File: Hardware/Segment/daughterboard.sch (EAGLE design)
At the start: 71 parts, among them IC1 PBQ79656PAPTQ1, X1 5566-12, X2 5566-12, X3 5566-16

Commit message: LDOIN
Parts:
- added CCB20: 0.1uf, capacitor-wima:C2.5/2
- added CCB21: 0.22uf, capacitor-wima:C2.5/2
- added Q1: (no value), semicon-smd-ipc:NPN-TRANSISTIOR-2COLSOT143
- added RVC16: 49, rcl:R-US_R0603
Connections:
- removed net N$29: RCB10.1, RCB11.2, X2-11.S
- new net BATC: RCB10.1, RCB11.2, RVC16.2, X2-11.S
- new net GND: CCB21.1
- new net LDOIN: CCB20.2, IC1.LDOIN, Q1.E
- new net N$65: CCB21.2, Q1.C, RVC16.1
- new net NPNB: IC1.NPNB, Q1.B
- net GNDN: now also CCB20.1
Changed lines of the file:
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@@
 <part name="CCB18" library="capacitor-wima" library_urn="urn:adsk.eagle:library:116" deviceset="C" device="2.5/2" package3d_urn="urn:adsk.eagle:package:5415/1" value="220pf"/>
 <part name="CCB19" library="capacitor-wima" library_urn="urn:adsk.eagle:library:116" deviceset="C" device="2.5/2" package3d_urn="urn:adsk.eagle:package:5415/1" value="220pf"/>
+<part name="CCB20" library="capacitor-wima" library_urn="urn:adsk.eagle:library:116" deviceset="C" device="2.5/2" package3d_urn="urn:adsk.eagle:package:5415/1" value="0.1uf"/>
+<part name="Q1" library="semicon-smd-ipc" library_urn="urn:adsk.eagle:library:353" deviceset="NPN-TRANSISTIOR-2COL" device="SOT143" package3d_urn="urn:adsk.eagle:package:26315/2"/>
+<part name="RVC16" library="rcl" library_urn="urn:adsk.eagle:library:334" deviceset="R-US_" device="R0603" package3d_urn="urn:adsk.eagle:package:23555/3" value="49"/>
+<part name="CCB21" library="capacitor-wima" library_urn="urn:adsk.eagle:library:116" deviceset="C" device="2.5/2" package3d_urn="urn:adsk.eagle:package:5415/1" value="0.22uf"/>
+<part name="GND1" library="supply1" library_urn="urn:adsk.eagle:library:371" deviceset="GND" device=""/>
 </parts>
 <sheets>
@@
 <attribute name="NAME" x="170.561" y="6.096" size="1.778" layer="95" rot="R270"/>
 <attribute name="VALUE" x="165.481" y="6.096" size="1.778" layer="96" rot="R270"/>
+</instance>
+<instance part="CCB20" gate="G$1" x="116.84" y="7.62" smashed="yes" rot="R90">
+<attribute name="NAME" x="116.459" y="9.144" size="1.778" layer="95" rot="R90"/>
+<attribute name="VALUE" x="121.539" y="9.144" size="1.778" layer="96" rot="R90"/>
+</instance>
+<instance part="Q1" gate="G$1" x="127" y="-2.54" smashed="yes" rot="R180">
+<attribute name="NAME" x="137.16" y="-5.08" size="1.778" layer="95" rot="R180"/>
+<attribute name="VALUE" x="137.16" y="-7.62" size="1.778" layer="96" rot="R180"/>
+</instance>
+<instance part="RVC16" gate="G$1" x="109.22" y="-7.62" smashed="yes" rot="R180">
+<attribute name="NAME" x="113.03" y="-9.1186" size="1.778" layer="95" rot="R180"/>
+<attribute name="VALUE" x="113.03" y="-4.318" size="1.778" layer="96" rot="R180"/>
+</instance>
+<instance part="CCB21" gate="G$1" x="106.68" y="0" smashed="yes" rot="R90">
+<attribute name="NAME" x="106.299" y="1.524" size="1.778" layer="95" rot="R90"/>
+<attribute name="VALUE" x="111.379" y="1.524" size="1.778" layer="96" rot="R90"/>
+</instance>
+<instance part="GND1" gate="1" x="93.98" y="0" smashed="yes" rot="R270">
+<attribute name="VALUE" x="91.44" y="2.54" size="1.778" layer="96" rot="R270"/>
 </instance>
 </instances>
@@
 <pinref part="RVC10" gate="G$1" pin="2"/>
 <wire x1="71.12" y1="111.76" x2="71.12" y2="116.84" width="0.1524" layer="91"/>
-</segment>
-</net>
-<net name="N$29" class="0">
-<segment>
-<pinref part="RCB10" gate="G$1" pin="1"/>
-<wire x1="45.72" y1="119.38" x2="71.12" y2="119.38" width="0.1524" layer="91"/>
-<pinref part="X2" gate="-11" pin="S"/>
-<wire x1="45.72" y1="119.38" x2="45.72" y2="124.46" width="0.1524" layer="91"/>
-<junction x="45.72" y="119.38"/>
-<pinref part="RCB11" gate="G$1" pin="2"/>
-<wire x1="45.72" y1="124.46" x2="177.8" y2="124.46" width="0.1524" layer="91"/>
-<wire x1="177.8" y1="124.46" x2="177.8" y2="104.14" width="0.1524" layer="91"/>
 </segment>
 </net>
@@
 <junction x="175.26" y="20.32"/>
 </segment>
+<segment>
+<pinref part="CCB20" gate="G$1" pin="1"/>
+<wire x1="114.3" y1="7.62" x2="93.98" y2="7.62" width="0.1524" layer="91"/>
+<label x="101.6" y="10.16" size="1.778" layer="95" rot="R180"/>
+</segment>
 </net>
 <net name="N$46" class="0">
@@
 </segment>
 </net>
+<net name="N$65" class="0">
+<segment>
+<pinref part="Q1" gate="G$1" pin="C"/>
+<pinref part="RVC16" gate="G$1" pin="1"/>
+<wire x1="124.46" y1="-7.62" x2="116.84" y2="-7.62" width="0.1524" layer="91"/>
+<wire x1="116.84" y1="-7.62" x2="114.3" y2="-7.62" width="0.1524" layer="91"/>
+<wire x1="116.84" y1="-7.62" x2="116.84" y2="0" width="0.1524" layer="91"/>
+<junction x="116.84" y="-7.62"/>
+<wire x1="116.84" y1="0" x2="111.76" y2="0" width="0.1524" layer="91"/>
+<pinref part="CCB21" gate="G$1" pin="2"/>
+</segment>
+</net>
+<net name="BATC" class="0">
+<segment>
+<pinref part="RVC16" gate="G$1" pin="2"/>
+<wire x1="104.14" y1="-7.62" x2="93.98" y2="-7.62" width="0.1524" layer="91"/>
+<label x="93.98" y="-7.62" size="1.778" layer="95"/>
+</segment>
+<segment>
+<pinref part="RCB10" gate="G$1" pin="1"/>
+<wire x1="45.72" y1="119.38" x2="71.12" y2="119.38" width="0.1524" layer="91"/>
+<pinref part="X2" gate="-11" pin="S"/>
+<wire x1="45.72" y1="119.38" x2="45.72" y2="124.46" width="0.1524" layer="91"/>
+<junction x="45.72" y="119.38"/>
+<pinref part="RCB11" gate="G$1" pin="2"/>
+<wire x1="45.72" y1="124.46" x2="177.8" y2="124.46" width="0.1524" layer="91"/>
+<wire x1="177.8" y1="124.46" x2="177.8" y2="104.14" width="0.1524" layer="91"/>
+<wire x1="177.8" y1="124.46" x2="190.5" y2="124.46" width="0.1524" layer="91"/>
+<junction x="177.8" y="124.46"/>
+<label x="185.42" y="124.46" size="1.778" layer="95"/>
+</segment>
+</net>
+<net name="LDOIN" class="0">
+<segment>
+<pinref part="IC1" gate="G$1" pin="LDOIN"/>
+<wire x1="175.26" y1="27.94" x2="175.26" y2="22.86" width="0.1524" layer="91"/>
+<label x="175.26" y="22.86" size="1.778" layer="95" rot="R90"/>
+</segment>
+<segment>
+<pinref part="Q1" gate="G$1" pin="E"/>
+<wire x1="124.46" y1="2.54" x2="124.46" y2="7.62" width="0.1524" layer="91"/>
+<pinref part="CCB20" gate="G$1" pin="2"/>
+<wire x1="124.46" y1="7.62" x2="121.92" y2="7.62" width="0.1524" layer="91"/>
+<wire x1="124.46" y1="7.62" x2="137.16" y2="7.62" width="0.1524" layer="91"/>
+<junction x="124.46" y="7.62"/>
+<label x="129.54" y="7.62" size="1.778" layer="95"/>
+</segment>
+</net>
+<net name="NPNB" class="0">
+<segment>
+<pinref part="IC1" gate="G$1" pin="NPNB"/>
+<wire x1="177.8" y1="27.94" x2="177.8" y2="22.86" width="0.1524" layer="91"/>
+<label x="177.8" y="22.86" size="1.778" layer="95" rot="R90"/>
+</segment>
+<segment>
+<pinref part="Q1" gate="G$1" pin="B"/>
+<wire x1="129.54" y1="-2.54" x2="137.16" y2="-2.54" width="0.1524" layer="91"/>
+<label x="129.54" y="-2.54" size="1.778" layer="95"/>
+</segment>
+</net>
+<net name="GND" class="0">
+<segment>
+<pinref part="CCB21" gate="G$1" pin="1"/>
+<pinref part="GND1" gate="1" pin="GND"/>
+<wire x1="104.14" y1="0" x2="96.52" y2="0" width="0.1524" layer="91"/>
+</segment>
+</net>

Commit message: NPN
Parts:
- removed Q1: (no value), semicon-smd-ipc:NPN-TRANSISTIOR-2COLSOT143
- added T1: PBHV8115X, 115, transistor:BC868-NPN-SOT89-BCE
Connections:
- net N$49 renamed CVDD
- net LDOIN: now also T1.E; no longer Q1.E
- net N$65: now also T1.C; no longer Q1.C
- net NPNB: now also T1.B; no longer Q1.B
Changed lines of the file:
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@@
 <part name="CCB19" library="capacitor-wima" library_urn="urn:adsk.eagle:library:116" deviceset="C" device="2.5/2" package3d_urn="urn:adsk.eagle:package:5415/1" value="220pf"/>
 <part name="CCB20" library="capacitor-wima" library_urn="urn:adsk.eagle:library:116" deviceset="C" device="2.5/2" package3d_urn="urn:adsk.eagle:package:5415/1" value="0.1uf"/>
-<part name="Q1" library="semicon-smd-ipc" library_urn="urn:adsk.eagle:library:353" deviceset="NPN-TRANSISTIOR-2COL" device="SOT143" package3d_urn="urn:adsk.eagle:package:26315/2"/>
 <part name="RVC16" library="rcl" library_urn="urn:adsk.eagle:library:334" deviceset="R-US_" device="R0603" package3d_urn="urn:adsk.eagle:package:23555/3" value="49"/>
 <part name="CCB21" library="capacitor-wima" library_urn="urn:adsk.eagle:library:116" deviceset="C" device="2.5/2" package3d_urn="urn:adsk.eagle:package:5415/1" value="0.22uf"/>
-<part name="GND1" library="supply1" library_urn="urn:adsk.eagle:library:371" deviceset="GND" device=""/>
+<part name="T1" library="transistor" library_urn="urn:adsk.eagle:library:402" deviceset="*-NPN-" device="SOT89-BCE" package3d_urn="urn:adsk.eagle:package:29925/3" technology="BC868" value="PBHV8115X, 115"/>
 </parts>
 <sheets>
@@
 <attribute name="VALUE" x="121.539" y="9.144" size="1.778" layer="96" rot="R90"/>
 </instance>
-<instance part="Q1" gate="G$1" x="127" y="-2.54" smashed="yes" rot="R180">
-<attribute name="NAME" x="137.16" y="-5.08" size="1.778" layer="95" rot="R180"/>
-<attribute name="VALUE" x="137.16" y="-7.62" size="1.778" layer="96" rot="R180"/>
-</instance>
 <instance part="RVC16" gate="G$1" x="109.22" y="-7.62" smashed="yes" rot="R180">
 <attribute name="NAME" x="113.03" y="-9.1186" size="1.778" layer="95" rot="R180"/>
@@
 <attribute name="VALUE" x="111.379" y="1.524" size="1.778" layer="96" rot="R90"/>
 </instance>
-<instance part="GND1" gate="1" x="93.98" y="0" smashed="yes" rot="R270">
-<attribute name="VALUE" x="91.44" y="2.54" size="1.778" layer="96" rot="R270"/>
+<instance part="T1" gate="G$1" x="127" y="-2.54" smashed="yes" rot="R180">
+<attribute name="NAME" x="137.16" y="-10.16" size="1.778" layer="95" rot="R180"/>
+<attribute name="VALUE" x="137.16" y="-7.62" size="1.778" layer="96" rot="R180"/>
 </instance>
 </instances>
@@
 <pinref part="CCB20" gate="G$1" pin="1"/>
 <wire x1="114.3" y1="7.62" x2="93.98" y2="7.62" width="0.1524" layer="91"/>
-<label x="101.6" y="10.16" size="1.778" layer="95" rot="R180"/>
+<label x="93.98" y="7.62" size="1.778" layer="95"/>
 </segment>
 </net>
@@
 <pinref part="CCB13" gate="G$1" pin="2"/>
 <pinref part="IC1" gate="G$1" pin="NEG5V"/>
-</segment>
-</net>
-<net name="N$49" class="0">
-<segment>
-<pinref part="CCB14" gate="G$1" pin="2"/>
-<pinref part="IC1" gate="G$1" pin="CVDD"/>
-<wire x1="170.18" y1="27.94" x2="170.18" y2="43.18" width="0.1524" layer="91"/>
-<junction x="170.18" y="27.94"/>
-<pinref part="IC1" gate="G$1" pin="RX"/>
-<wire x1="170.18" y1="43.18" x2="190.5" y2="43.18" width="0.1524" layer="91"/>
 </segment>
 </net>
@@
 <net name="N$65" class="0">
 <segment>
-<pinref part="Q1" gate="G$1" pin="C"/>
 <pinref part="RVC16" gate="G$1" pin="1"/>
 <wire x1="124.46" y1="-7.62" x2="116.84" y2="-7.62" width="0.1524" layer="91"/>
@@
 <wire x1="116.84" y1="0" x2="111.76" y2="0" width="0.1524" layer="91"/>
 <pinref part="CCB21" gate="G$1" pin="2"/>
+<pinref part="T1" gate="G$1" pin="C"/>
 </segment>
 </net>
@@
 </segment>
 <segment>
-<pinref part="Q1" gate="G$1" pin="E"/>
 <wire x1="124.46" y1="2.54" x2="124.46" y2="7.62" width="0.1524" layer="91"/>
 <pinref part="CCB20" gate="G$1" pin="2"/>
@@
 <junction x="124.46" y="7.62"/>
 <label x="129.54" y="7.62" size="1.778" layer="95"/>
+<pinref part="T1" gate="G$1" pin="E"/>
 </segment>
 </net>
@@
 </segment>
 <segment>
-<pinref part="Q1" gate="G$1" pin="B"/>
 <wire x1="129.54" y1="-2.54" x2="137.16" y2="-2.54" width="0.1524" layer="91"/>
 <label x="129.54" y="-2.54" size="1.778" layer="95"/>
+<pinref part="T1" gate="G$1" pin="B"/>
+</segment>
+</net>
+<net name="CVDD" class="0">
+<segment>
+<pinref part="IC1" gate="G$1" pin="RX"/>
+<wire x1="190.5" y1="43.18" x2="170.18" y2="43.18" width="0.1524" layer="91"/>
+<pinref part="CCB14" gate="G$1" pin="2"/>
+<pinref part="IC1" gate="G$1" pin="CVDD"/>
+<wire x1="170.18" y1="43.18" x2="170.18" y2="27.94" width="0.1524" layer="91"/>
+<junction x="170.18" y="27.94"/>
 </segment>
 </net>
@@
 <segment>
 <pinref part="CCB21" gate="G$1" pin="1"/>
-<pinref part="GND1" gate="1" pin="GND"/>
-<wire x1="104.14" y1="0" x2="96.52" y2="0" width="0.1524" layer="91"/>
-</segment>
-</net>
+<wire x1="104.14" y1="0" x2="93.98" y2="0" width="0.1524" layer="91"/>
+<label x="93.98" y="0" size="1.778" layer="95"/>
+</segment>
+</net>

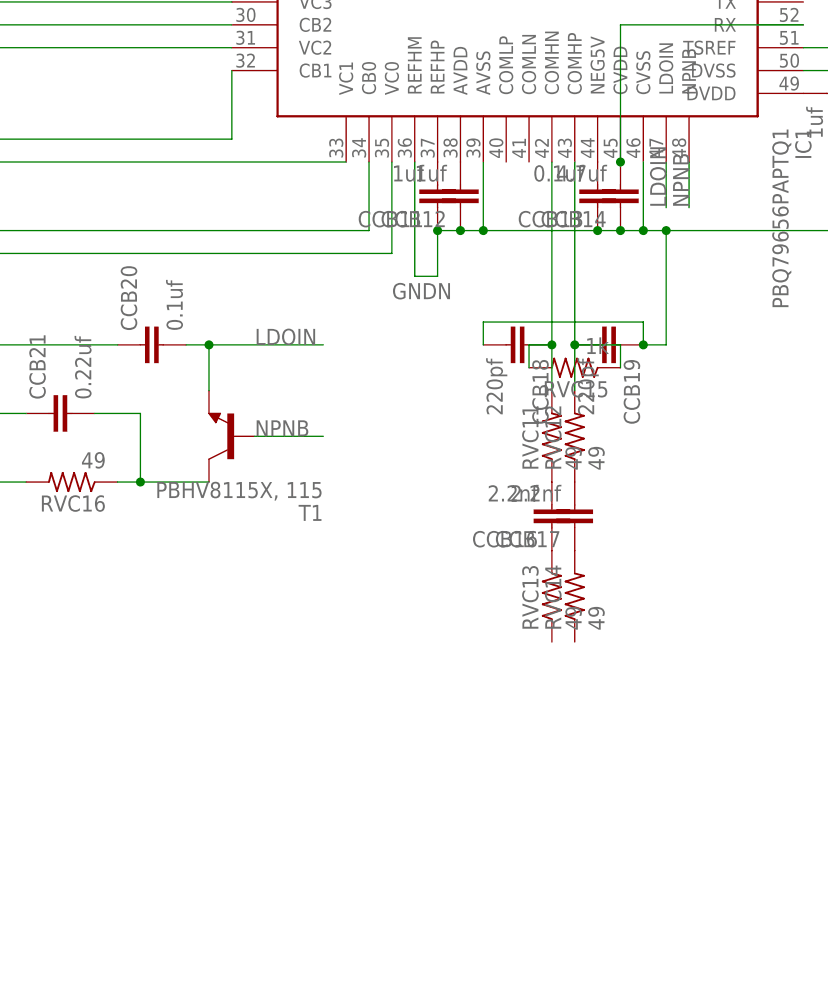
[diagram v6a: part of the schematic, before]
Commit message: added COMLP and COMLN connection
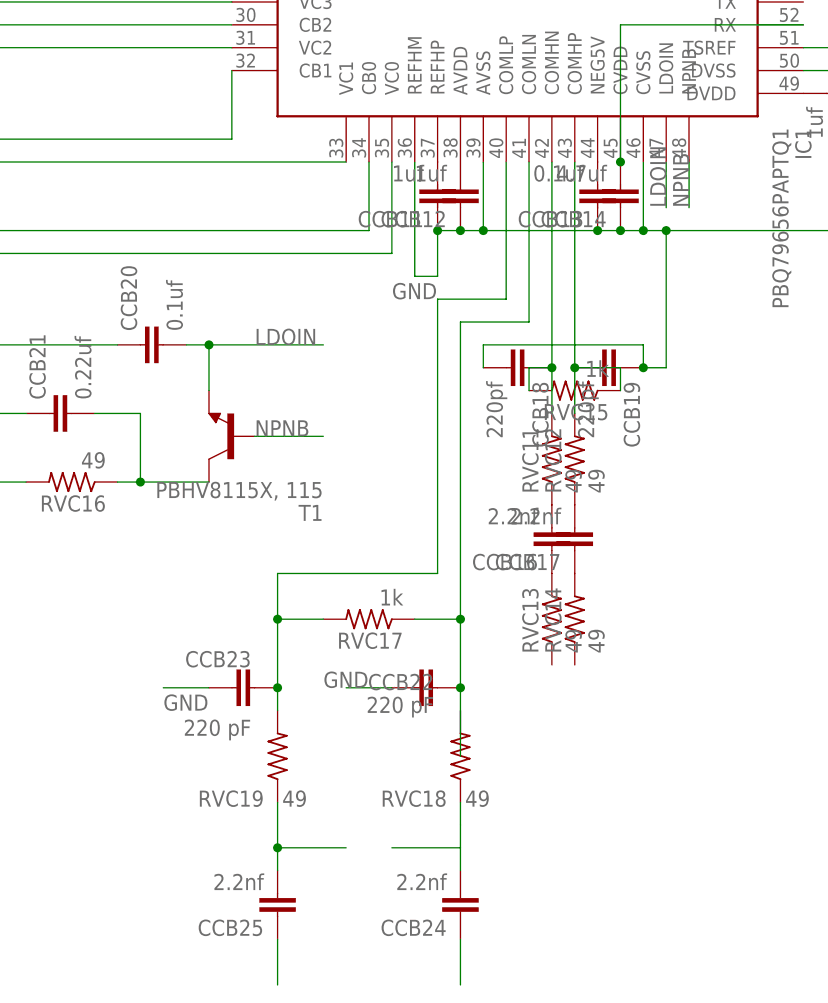
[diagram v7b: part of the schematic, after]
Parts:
- added CCB22, CCB23: 220 pF, capacitor-wima:C2.5/2
- added CCB24, CCB25: 2.2nf, capacitor-wima:C2.5/2
- added RVC17: 1k, rcl:R-US_R0603
- added RVC18, RVC19: 49, rcl:R-US_R0603
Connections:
- new net N$29: CCB22.2, IC1.COMLN, RVC17.1, RVC18.2
- new net N$49: CCB23.2, IC1.COMLP, RVC17.2, RVC19.2
- new net N$66: CCB25.1
- new net N$67: CCB25.2, RVC19.1
- new net N$68: CCB24.2, RVC18.1
- new net N$69: CCB24.1
- net GND: now also CCB11.1, CCB12.1, CCB13.1, CCB14.1, CCB15.1, CCB18.2, CCB19.1, CCB22.1, CCB23.1, IC1.AVSS, IC1.AVSS?, IC1.CVSS, IC1.DVSS, IC1.REFHM
- net GNDN: no longer CCB11.1, CCB12.1, CCB13.1, CCB14.1, CCB15.1, CCB18.2, CCB19.1, IC1.AVSS, IC1.AVSS?, IC1.CVSS, IC1.DVSS, IC1.REFHM
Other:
- moved on the sheet: CCB16, CCB17, CCB18, CCB19, RVC11, RVC12, RVC13, RVC14, RVC15

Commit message: Finished daughterboard schematic?
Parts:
- added C2, C3: 1 uF, capacitor-wima:C2.5/2
- added CCB26, CCB27, CCB28, CCB29, CCB30, CCB31, CCB32, CCB33, CCB34, CCB35, CCB52, CCB53, CCB54, CCB55, CCB56, CCB57, CCB58, CCB59, CCB60, CCB61, CVC10, CVC11, CVC12, CVC13, CVC14, CVC15, CVC16, CVC17, CVC18, CVC19, CVC20, CVC21, CVC22, CVC23, CVC24, CVC25, CVC26, CVC27, CVC28, CVC29: 0.47uf, capacitor-wima:C2.5/2
- added CCB36, CCB62: 10 nf, capacitor-wima:C2.5/2
- added CCB37, CCB38, CCB41, CCB63, CCB64, CCB67: 1uf, capacitor-wima:C2.5/2
- added CCB39, CCB46, CCB65, CCB68: 0.1uf, capacitor-wima:C2.5/2
- added CCB40, CCB66: 4.7uf, capacitor-wima:C2.5/2
- added CCB42, CCB43, CCB49, CCB50, CCB71, CCB72: 2.2nf, capacitor-wima:C2.5/2
- added CCB44, CCB45, CCB74, CCB75: 220pf, capacitor-wima:C2.5/2
- added CCB47, CCB69: 0.22uf, capacitor-wima:C2.5/2
- added CCB48, CCB51, CCB70, CCB73: 220 pF, capacitor-wima:C2.5/2
- added D1, D2, D3: ESDAVLC6-2BLY, ESDAVLC6-2BLY:ESDAVLC6-2BLY
- added IC2, IC3: PBQ79656PAPTQ1, PBQ79656PAPTQ1:PBQ79656PAPTQ1
- added R10, R11, R12, R13, R14, R15, R16, R17, R18, R19, R20, R21, R22, R23, R24, R9: 10k, rcl:R-US_R0603
- added RCB12, RCB13, RCB14, RCB15, RCB16, RCB17, RCB18, RCB19, RCB20, RCB21, RCB22, RCB24, RCB25, RCB26, RCB27, RCB28, RCB29, RCB30, RCB31, RCB32, RCB33, RCB34: 10, rcl:R-US_R0603
- added RCB23, RCB35: 30, rcl:R-US_R0603
- added RVC20, RVC21, RVC22, RVC23, RVC24, RVC25, RVC26, RVC27, RVC28, RVC29, RVC30, RVC40, RVC41, RVC42, RVC43, RVC44, RVC45, RVC46, RVC47, RVC48, RVC49, RVC50: 100, rcl:R-US_R0603
- added RVC31, RVC32, RVC33, RVC34, RVC36, RVC38, RVC39, RVC51, RVC53, RVC54: 49, rcl:R-US_R0603
- added RVC35, RVC37, RVC52, RVC55: 1k, rcl:R-US_R0603
- added T2, T3: PBHV8115X, 115, transistor:BC868-NPN-SOT89-BCE
- added X4, X5, X7, X8: 5566-12, con-molex:5566-12
- added X6, X9: 5566-16, con-molex:5566-16
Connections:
- new net BATC-1: RCB21.1, RCB23.2, RCB33.1, RCB35.2, RVC36.2, RVC51.2, X5-11.S, X8-11.S
- new net COMMN: CCB74.1, IC3.COMLN, RVC33.1, RVC55.2
- new net COMMP: CCB75.2, IC3.COMLP, RVC34.1, RVC55.1
- new net CVDD-1: CCB40.2, IC2.CVDD, IC2.RX
- new net CVDD2: CCB66.2, IC3.CVDD, IC3.RX
- new net GND-1: CCB37.1, CCB38.1, CCB39.1, CCB40.1, CCB41.1, CCB44.2, CCB45.1, CCB47.1, CCB48.1, CCB51.1, CCB63.1, CCB64.1, CCB65.1, CCB66.1, CCB67.1, CCB69.1, CCB70.1, CCB73.1, CCB74.2, CCB75.1, D2.3, D3.3, IC2.AVSS, IC2.AVSS?, IC2.CVSS, IC2.DVSS, IC2.REFHM, IC3.AVSS, IC3.AVSS?, IC3.CVSS, IC3.DVSS, IC3.REFHM
- new net GND1-1: C2.1, C3.1, CCB36.1, CCB62.1, RCB22.1, RCB34.1, X5-1.S, X6-10.S, X6-11.S, X6-12.S, X6-13.S, X6-14.S, X6-15.S, X6-16.S, X6-9.S, X8-1.S, X9-10.S, X9-11.S, X9-12.S, X9-13.S, X9-14.S, X9-15.S, X9-16.S, X9-9.S
- new net GNDN-1: CCB46.1, CCB68.1
- new net LDOIN-1: CCB46.2, CCB68.2, IC2.LDOIN, IC3.LDOIN, T2.E, T3.E
- new net N$100: CCB35.2, IC2.CB0, RCB22.2
- new net N$101: CVC19.2, RVC30.1, X4-1.S
- new net N$102: CVC10.2, CVC19.1, RVC20.1, X4-2.S
- new net N$103: CVC10.1, CVC11.2, RVC21.1, X4-3.S
- new net N$104: CVC11.1, CVC12.2, RVC22.1, X4-4.S
- new net N$105: CVC12.1, CVC13.2, RVC23.1, X4-5.S
- new net N$106: CVC13.1, CVC14.2, RVC24.1, X4-6.S
- new net N$107: CVC14.1, CVC15.2, RVC25.1, X4-7.S
- new net N$108: CVC15.1, CVC16.2, RVC26.1, X4-8.S
- new net N$109: CVC16.1, CVC17.2, RVC27.1, X4-9.S
- new net N$110: CVC17.1, CVC18.2, RVC28.1, X4-10.S
- new net N$111: CVC18.1, RVC29.1, X4-11.S
- new net N$112: CCB36.2, IC2.BAT, IC2.CB11, IC2.CB12, IC2.CB13, IC2.CB14, IC2.CB15, IC2.CB16, IC2.VC11, IC2.VC12, IC2.VC13, IC2.VC14, IC2.VC15, IC2.VC16, RCB23.1
- new net N$113: CCB37.2, IC2.REFHP
- new net N$114: CCB38.2, IC2.AVDD
- new net N$115: CCB39.2, IC2.NEG5V
- new net N$116: CCB41.2, IC2.DVDD
- new net N$117: IC2.GPIO1, R16.2, X6-1.S
- new net N$118: IC2.GPIO2, R15.2, X6-2.S
- new net N$119: IC2.GPIO3, R14.2, X6-3.S
- new net N$120: IC2.GPIO4, R13.2, X6-4.S
- new net N$121: IC2.GPIO5, R12.2, X6-5.S
- new net N$122: IC2.GPIO6, R11.2, X6-6.S
- new net N$123: IC2.GPIO7, R10.2, X6-7.S
- new net N$124: IC2.GPIO8, R9.2, X6-8.S
- new net N$125: C2.2, IC2.TSREF, R10.1, R11.1, R12.1, R13.1, R14.1, R15.1, R16.1, R9.1
- new net N$126: CCB44.1, IC2.COMHN, RVC31.2, RVC35.2
- new net N$127: CCB45.2, IC2.COMHP, RVC32.2, RVC35.1
- new net N$128: CCB42.2, RVC31.1
- new net N$129: CCB43.2, RVC32.1
- new net N$130: CCB42.1, RVC33.2
- new net N$131: CCB43.1, RVC34.2
- new net N$132: CCB47.2, RVC36.1, T2.C
- new net N$133: CCB48.2, IC2.COMLN, RVC37.1, RVC38.2
- new net N$134: CCB51.2, IC2.COMLP, RVC37.2, RVC39.2
- new net N$135: CCB50.2, D2.2, RVC39.1
- new net N$136: CCB49.2, D2.1, RVC38.1
- new net N$137: CCB49.1
- new net N$138: CCB50.1
- new net N$139: IC3.VC1, RVC40.2
- new net N$140: CCB52.2, CCB61.1, IC3.CB1, RCB24.2
- new net N$141: IC3.VC2, RVC41.2
- new net N$142: CCB52.1, CCB53.2, IC3.CB2, RCB25.2
- new net N$143: RCB25.1, X8-3.S
- new net N$144: RCB24.1, X8-2.S
- new net N$145: CCB53.1, CCB54.2, IC3.CB3, RCB26.2
- new net N$146: RCB26.1, X8-4.S
- new net N$147: IC3.VC3, RVC42.2
- new net N$148: IC3.VC4, RVC43.2
- new net N$149: RCB27.1, X8-5.S
- new net N$150: CCB54.1, CCB55.2, IC3.CB4, RCB27.2
- new net N$151: IC3.VC5, RVC44.2
- new net N$152: RCB28.1, X8-6.S
- new net N$153: CCB55.1, CCB56.2, IC3.CB5, RCB28.2
- new net N$154: IC3.VC6, RVC45.2
- new net N$155: RCB29.1, X8-7.S
- new net N$156: CCB56.1, CCB57.2, IC3.CB6, RCB29.2
- new net N$157: IC3.VC7, RVC46.2
- new net N$158: RCB30.1, X8-8.S
- new net N$159: CCB57.1, CCB58.2, IC3.CB7, RCB30.2
- new net N$160: IC3.VC8, RVC47.2
- new net N$161: RCB31.1, X8-9.S
- new net N$162: CCB58.1, CCB59.2, IC3.CB8, RCB31.2
- new net N$163: IC3.VC9, RVC48.2
- new net N$164: RCB32.1, X8-10.S
- new net N$165: CCB59.1, CCB60.2, IC3.CB9, RCB32.2
- new net N$166: IC3.VC10, RVC49.2
- new net N$167: CCB60.1, IC3.CB10, RCB33.2
- new net N$168: IC3.VC0, RVC50.2
- new net N$169: CCB61.2, IC3.CB0, RCB34.2
- new net N$170: CVC29.2, RVC50.1, X7-1.S
- new net N$171: CVC20.2, CVC29.1, RVC40.1, X7-2.S
- new net N$172: CVC20.1, CVC21.2, RVC41.1, X7-3.S
- new net N$173: CVC21.1, CVC22.2, RVC42.1, X7-4.S
- new net N$174: CVC22.1, CVC23.2, RVC43.1, X7-5.S
- new net N$175: CVC23.1, CVC24.2, RVC44.1, X7-6.S
- new net N$176: CVC24.1, CVC25.2, RVC45.1, X7-7.S
- new net N$177: CVC25.1, CVC26.2, RVC46.1, X7-8.S
- new net N$178: CVC26.1, CVC27.2, RVC47.1, X7-9.S
- new net N$179: CVC27.1, CVC28.2, RVC48.1, X7-10.S
- new net N$180: CVC28.1, RVC49.1, X7-11.S
- new net N$181: CCB62.2, IC3.BAT, IC3.CB11, IC3.CB12, IC3.CB13, IC3.CB14, IC3.CB15, IC3.CB16, IC3.VC11, IC3.VC12, IC3.VC13, IC3.VC14, IC3.VC15, IC3.VC16, RCB35.1
- new net N$182: CCB63.2, IC3.REFHP
- new net N$183: CCB64.2, IC3.AVDD
- new net N$184: CCB65.2, IC3.NEG5V
- new net N$185: CCB67.2, IC3.DVDD
- new net N$186: IC3.GPIO1, R24.2, X9-1.S
- new net N$187: IC3.GPIO2, R23.2, X9-2.S
- new net N$188: IC3.GPIO3, R22.2, X9-3.S
- new net N$189: IC3.GPIO4, R21.2, X9-4.S
- new net N$190: IC3.GPIO5, R20.2, X9-5.S
- new net N$191: IC3.GPIO6, R19.2, X9-6.S
- new net N$192: IC3.GPIO7, R18.2, X9-7.S
- new net N$193: IC3.GPIO8, R17.2, X9-8.S
- new net N$194: C3.2, IC3.TSREF, R17.1, R18.1, R19.1, R20.1, R21.1, R22.1, R23.1, R24.1
- new net N$195: CCB69.2, RVC51.1, T3.C
- new net N$198: CCB72.2, D3.2, RVC54.1
- new net N$199: CCB71.2, D3.1, RVC53.1
- new net N$200: CCB71.1
- new net N$201: CCB72.1
- new net N$202: CCB73.2, IC3.COMHN, RVC52.2, RVC54.2
- new net N$203: CCB70.2, IC3.COMHP, RVC52.1, RVC53.2
- new net N$70: IC2.VC1, RVC20.2
- new net N$71: CCB26.2, CCB35.1, IC2.CB1, RCB12.2
- new net N$72: IC2.VC2, RVC21.2
- new net N$73: CCB26.1, CCB27.2, IC2.CB2, RCB13.2
- new net N$74: RCB13.1, X5-3.S
- new net N$75: RCB12.1, X5-2.S
- new net N$76: CCB27.1, CCB28.2, IC2.CB3, RCB14.2
- new net N$77: RCB14.1, X5-4.S
- new net N$78: IC2.VC3, RVC22.2
- new net N$79: IC2.VC4, RVC23.2
- new net N$80: RCB15.1, X5-5.S
- new net N$81: CCB28.1, CCB29.2, IC2.CB4, RCB15.2
- new net N$82: IC2.VC5, RVC24.2
- new net N$83: RCB16.1, X5-6.S
- new net N$84: CCB29.1, CCB30.2, IC2.CB5, RCB16.2
- new net N$85: IC2.VC6, RVC25.2
- new net N$86: RCB17.1, X5-7.S
- new net N$87: CCB30.1, CCB31.2, IC2.CB6, RCB17.2
- new net N$88: IC2.VC7, RVC26.2
- new net N$89: RCB18.1, X5-8.S
- new net N$90: CCB31.1, CCB32.2, IC2.CB7, RCB18.2
- new net N$91: IC2.VC8, RVC27.2
- new net N$92: RCB19.1, X5-9.S
- new net N$93: CCB32.1, CCB33.2, IC2.CB8, RCB19.2
- new net N$94: IC2.VC9, RVC28.2
- new net N$95: RCB20.1, X5-10.S
- new net N$96: CCB33.1, CCB34.2, IC2.CB9, RCB20.2
- new net N$97: IC2.VC10, RVC29.2
- new net N$98: CCB34.1, IC2.CB10, RCB21.2
- new net N$99: IC2.VC0, RVC30.2
- new net NPNB-1: IC2.NPNB, IC3.NPNB, T2.B, T3.B
- net GND: now also D1.3
- net N$67: now also D1.2
- net N$68: now also D1.1
